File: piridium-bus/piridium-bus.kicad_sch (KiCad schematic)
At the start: 53 parts, among them J1 EPS, J2 MODEM UART, J3 ANT, J4 PAYLOAD, Q1 2N7002, Q2 DMP3015LSSQ, U1 LM1117-3.3, U2 TPS54394RSAR, U3 MAX6369, U4 74LS126, U5 DS3232M

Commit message: update routing
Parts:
- removed J4: PAYLOAD, Connector_Molex:Molex_Nano-Fit_105314-xx10_2x05_P2.50mm_Horizontal, symbol Connector_Generic:Conn_02x05_Top_Bottom
- added J4: PAYLOAD, Connector_PinHeader_2.54mm:PinHeader_2x05_P2.54mm_Vertical, symbol Connector_Generic:Conn_02x05_Odd_Even
- J1: footprint Connector_Molex:Molex_Nano-Fit_105313-xx04_1x04_P2.50mm_Horizontal -> Connector_PinHeader_2.54mm:PinHeader_1x04_P2.54mm_Horizontal
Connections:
- net +5V: no longer R9.1
- net +5VP: now also R9.1
- net GND: now also J4.10 (Pin_10), J4.9 (Pin_9); no longer A3.22 (RF_GND), J3.2 (Ext)
- net I2C_SCL: now also J4.2 (Pin_2)
- net I2C_SDA: now also J4.4 (Pin_4)
- net PAYLOAD_PWR: now also J4.1 (Pin_1)
- net SPI_CE0: now also J4.6 (Pin_6)
- net SPI_CE1: now also J4.8 (Pin_8)
- net SPI_MISO: now also J4.5 (Pin_5)
- net SPI_MOSI: now also J4.3 (Pin_3)
- net SPI_SCK: now also J4.7 (Pin_7)
- new net GNDS: A3.22 (RF_GND), J3.2 (Ext)
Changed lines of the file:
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@@
   (junction (at 248.92 55.88) (diameter 0) (color 0 0 0 0)
   )
-  (junction (at 236.22 133.35) (diameter 0) (color 0 0 0 0)
-  )
   (junction (at 20.32 114.3) (diameter 0) (color 0 0 0 0)
   )
@@
   (junction (at 50.8 50.8) (diameter 0) (color 0 0 0 0)
   )
-  (junction (at 236.22 125.73) (diameter 0) (color 0 0 0 0)
-  )
   (junction (at 179.07 77.47) (diameter 0) (color 0 0 0 0)
   )
@@
   )
   (junction (at 63.5 60.96) (diameter 0) (color 0 0 0 0)
+  )
+  (junction (at 246.38 128.27) (diameter 0) (color 0 0 0 0)
   )
   (junction (at 33.02 33.02) (diameter 0) (color 0 0 0 0)
@@
     (stroke (width 0) (type default) (color 0 0 0 0))
   )
-  (wire (pts (xy 246.38 128.27) (xy 246.38 133.35))
-    (stroke (width 0) (type default) (color 0 0 0 0))
-  )
   (polyline (pts (xy 231.14 83.82) (xy 231.14 45.72))
     (stroke (width 0) (type default) (color 0 0 0 0))
@@
     (stroke (width 0) (type default) (color 0 0 0 0))
   )
+  (wire (pts (xy 232.41 125.73) (xy 241.3 125.73))
+    (stroke (width 0) (type default) (color 0 0 0 0))
+  )
   (wire (pts (xy 45.72 133.35) (xy 49.53 133.35))
     (stroke (width 0) (type default) (color 0 0 0 0))
@@
     (stroke (width 0) (type default) (color 0 0 0 0))
   )
-  (wire (pts (xy 246.38 133.35) (xy 236.22 133.35))
-    (stroke (width 0) (type default) (color 0 0 0 0))
-  )
   (polyline (pts (xy 289.56 44.45) (xy 289.56 13.97))
     (stroke (width 0) (type default) (color 0 0 0 0))
@@
     (stroke (width 0) (type default) (color 0 0 0 0))
   )
-  (wire (pts (xy 232.41 125.73) (xy 236.22 125.73))
-    (stroke (width 0) (type default) (color 0 0 0 0))
-  )
   (wire (pts (xy 175.26 22.86) (xy 179.07 22.86))
     (stroke (width 0) (type default) (color 0 0 0 0))
@@
     (stroke (width 0) (type default) (color 0 0 0 0))
   )
-  (wire (pts (xy 236.22 133.35) (xy 236.22 125.73))
+  (wire (pts (xy 236.22 113.03) (xy 236.22 133.35))
     (stroke (width 0) (type default) (color 0 0 0 0))
   )
@@
     (stroke (width 0) (type default) (color 0 0 0 0))
   )
+  (wire (pts (xy 241.3 125.73) (xy 241.3 128.27))
+    (stroke (width 0) (type default) (color 0 0 0 0))
+  )
   (wire (pts (xy 240.03 99.06) (xy 242.57 99.06))
     (stroke (width 0) (type default) (color 0 0 0 0))
@@
     (stroke (width 0) (type default) (color 0 0 0 0))
   )
-  (wire (pts (xy 236.22 125.73) (xy 236.22 113.03))
-    (stroke (width 0) (type default) (color 0 0 0 0))
-  )
   (wire (pts (xy 179.07 69.85) (xy 179.07 77.47))
     (stroke (width 0) (type default) (color 0 0 0 0))
@@
   )
   (wire (pts (xy 99.06 57.15) (xy 114.3 57.15))
+    (stroke (width 0) (type default) (color 0 0 0 0))
+  )
+  (wire (pts (xy 241.3 128.27) (xy 246.38 128.27))
     (stroke (width 0) (type default) (color 0 0 0 0))
   )
@@
     (pin "1")
   )
+  (symbol (lib_id "power:GNDS") (at 246.38 128.27 0) (unit 1)
+    (in_bom yes) (on_board yes) (fields_autoplaced)
+    (property "Reference" "#PWR0101" (id 0) (at 246.38 134.62 0)
+      (effects (font (size 1.27 1.27)) hide)
+    )
+    (property "Value" "GNDS" (id 1) (at 246.38 133.35 0))
+    (property "Footprint" "" (id 2) (at 246.38 128.27 0)
+      (effects (font (size 1.27 1.27)) hide)
+    )
+    (property "Datasheet" "" (id 3) (at 246.38 128.27 0)
+      (effects (font (size 1.27 1.27)) hide)
+    )
+    (pin "1")
+  )
   (symbol (lib_id "power:GND") (at 25.4 99.06 0) (unit 1)
     (in_bom yes) (on_board yes)
@@
       (effects (font (size 1.27 1.27)) (justify left))
     )
-    (property "Footprint" "Connector_Molex:Molex_Nano-Fit_105313-xx04_1x04_P2.50mm_Horizontal" (id 2) (at 20.32 93.98 0)
+    (property "Footprint" "Connector_PinHeader_2.54mm:PinHeader_1x04_P2.54mm_Horizontal" (id 2) (at 20.32 93.98 0)
       (effects (font (size 1.27 1.27)) hide)
     )
@@
     (pin "2")
   )
+  (symbol (lib_id "power:+5VP") (at 233.68 91.44 0) (unit 1)
+    (in_bom yes) (on_board yes) (fields_autoplaced)
+    (property "Reference" "#PWR?" (id 0) (at 233.68 95.25 0)
+      (effects (font (size 1.27 1.27)) hide)
+    )
+    (property "Value" "+5VP" (id 1) (at 233.68 86.36 0))
+    (property "Footprint" "" (id 2) (at 233.68 91.44 0)
+      (effects (font (size 1.27 1.27)) hide)
+    )
+    (property "Datasheet" "" (id 3) (at 233.68 91.44 0)
+      (effects (font (size 1.27 1.27)) hide)
+    )
+    (pin "1")
+  )
   (symbol (lib_id "power:+5V") (at 114.3 69.85 90) (unit 1)
     (in_bom yes) (on_board yes) (fields_autoplaced)
@@
     )
     (pin "1")
-  )
-  (symbol (lib_id "Connector_Generic:Conn_02x05_Top_Bottom") (at 270.51 35.56 0) (unit 1)
-    (in_bom yes) (on_board yes) (fields_autoplaced)
-    (property "Reference" "J4" (id 0) (at 271.78 24.13 0))
-    (property "Value" "PAYLOAD" (id 1) (at 271.78 26.67 0))
-    (property "Footprint" "Connector_Molex:Molex_Nano-Fit_105314-xx10_2x05_P2.50mm_Horizontal" (id 2) (at 270.51 35.56 0)
-      (effects (font (size 1.27 1.27)) hide)
-    )
-    (property "Datasheet" "~" (id 3) (at 270.51 35.56 0)
-      (effects (font (size 1.27 1.27)) hide)
-    )
-    (pin "1")
-    (pin "10")
-    (pin "2")
-    (pin "3")
-    (pin "4")
-    (pin "5")
-    (pin "6")
-    (pin "7")
-    (pin "8")
-    (pin "9")
   )
   (symbol (lib_id "power:GND") (at 203.2 77.47 0) (unit 1)
@@
     (pin "2")
   )
+  (symbol (lib_id "Connector_Generic:Conn_02x05_Odd_Even") (at 270.51 35.56 0) (unit 1)
+    (in_bom yes) (on_board yes) (fields_autoplaced)
+    (property "Reference" "J4" (id 0) (at 271.78 24.13 0))
+    (property "Value" "PAYLOAD" (id 1) (at 271.78 26.67 0))
+    (property "Footprint" "Connector_PinHeader_2.54mm:PinHeader_2x05_P2.54mm_Vertical" (id 2) (at 270.51 35.56 0)
+      (effects (font (size 1.27 1.27)) hide)
+    )
+    (property "Datasheet" "~" (id 3) (at 270.51 35.56 0)
+      (effects (font (size 1.27 1.27)) hide)
+    )
+    (pin "1")
+    (pin "10")
+    (pin "2")
+    (pin "3")
+    (pin "4")
+    (pin "5")
+    (pin "6")
+    (pin "7")
+    (pin "8")
+    (pin "9")
+  )
   (symbol (lib_id "Device:R") (at 234.95 21.59 0) (mirror y) (unit 1)
     (in_bom yes) (on_board yes)
@@
     (pin "1")
   )
-  (symbol (lib_id "power:+5V") (at 233.68 91.44 0) (unit 1)
-    (in_bom yes) (on_board yes) (fields_autoplaced)
-    (property "Reference" "#PWR028" (id 0) (at 233.68 95.25 0)
-      (effects (font (size 1.27 1.27)) hide)
-    )
-    (property "Value" "+5V" (id 1) (at 233.68 86.36 0))
-    (property "Footprint" "" (id 2) (at 233.68 91.44 0)
-      (effects (font (size 1.27 1.27)) hide)
-    )
-    (property "Datasheet" "" (id 3) (at 233.68 91.44 0)
-      (effects (font (size 1.27 1.27)) hide)
-    )
-    (pin "1")
-  )
   (symbol (lib_id "power:GND") (at 236.22 133.35 0) (unit 1)
     (in_bom yes) (on_board yes) (fields_autoplaced)
@@
       (reference "#PWR027") (unit 1) (value "GND") (footprint "")
     )
-    (path "/fb473a15-78ef-46d6-8141-4de438a4d939"
-      (reference "#PWR028") (unit 1) (value "+5V") (footprint "")
-    )
     (path "/2957e5e6-b93f-4726-81ca-ef39d24a291b"
       (reference "#PWR029") (unit 1) (value "GND") (footprint "")
@@
       (reference "#PWR036") (unit 1) (value "GND") (footprint "")
     )
+    (path "/2408a518-0026-450c-95ff-4703dcc60255"
+      (reference "#PWR0101") (unit 1) (value "GNDS") (footprint "")
+    )
+    (path "/733fde0d-fd57-4432-87d0-a513bd1e831a"
+      (reference "#PWR?") (unit 1) (value "+5VP") (footprint "")
+    )
     (path "/dee1721c-7498-4aa5-ba4d-8809f87db910"
       (reference "A1") (unit 1) (value "Raspberry_Pi_Zero") (footprint "piridium-bus:Raspberry Pi Zero")
@@
     )
     (path "/321ea199-1ef7-40a0-ade9-c079749b846a"
-      (reference "J1") (unit 1) (value "EPS") (footprint "Connector_Molex:Molex_Nano-Fit_105313-xx04_1x04_P2.50mm_Horizontal")
+      (reference "J1") (unit 1) (value "EPS") (footprint "Connector_PinHeader_2.54mm:PinHeader_1x04_P2.54mm_Horizontal")
     )
     (path "/8c75ddb9-a755-44c9-bc38-54adf2375e84"
@@
       (reference "J3") (unit 1) (value "ANT") (footprint "Connector_Coaxial:SMA_Amphenol_901-144_Vertical")
     )
-    (path "/c327fdf2-43a7-41a6-a455-95be41197291"
-      (reference "J4") (unit 1) (value "PAYLOAD") (footprint "Connector_Molex:Molex_Nano-Fit_105314-xx10_2x05_P2.50mm_Horizontal")
+    (path "/e777e5ce-0d5c-4bac-a8bd-4486133c1e81"
+      (reference "J4") (unit 1) (value "PAYLOAD") (footprint "Connector_PinHeader_2.54mm:PinHeader_2x05_P2.54mm_Vertical")
     )
     (path "/f194e39b-0e91-4755-8253-375d1bf0a961"

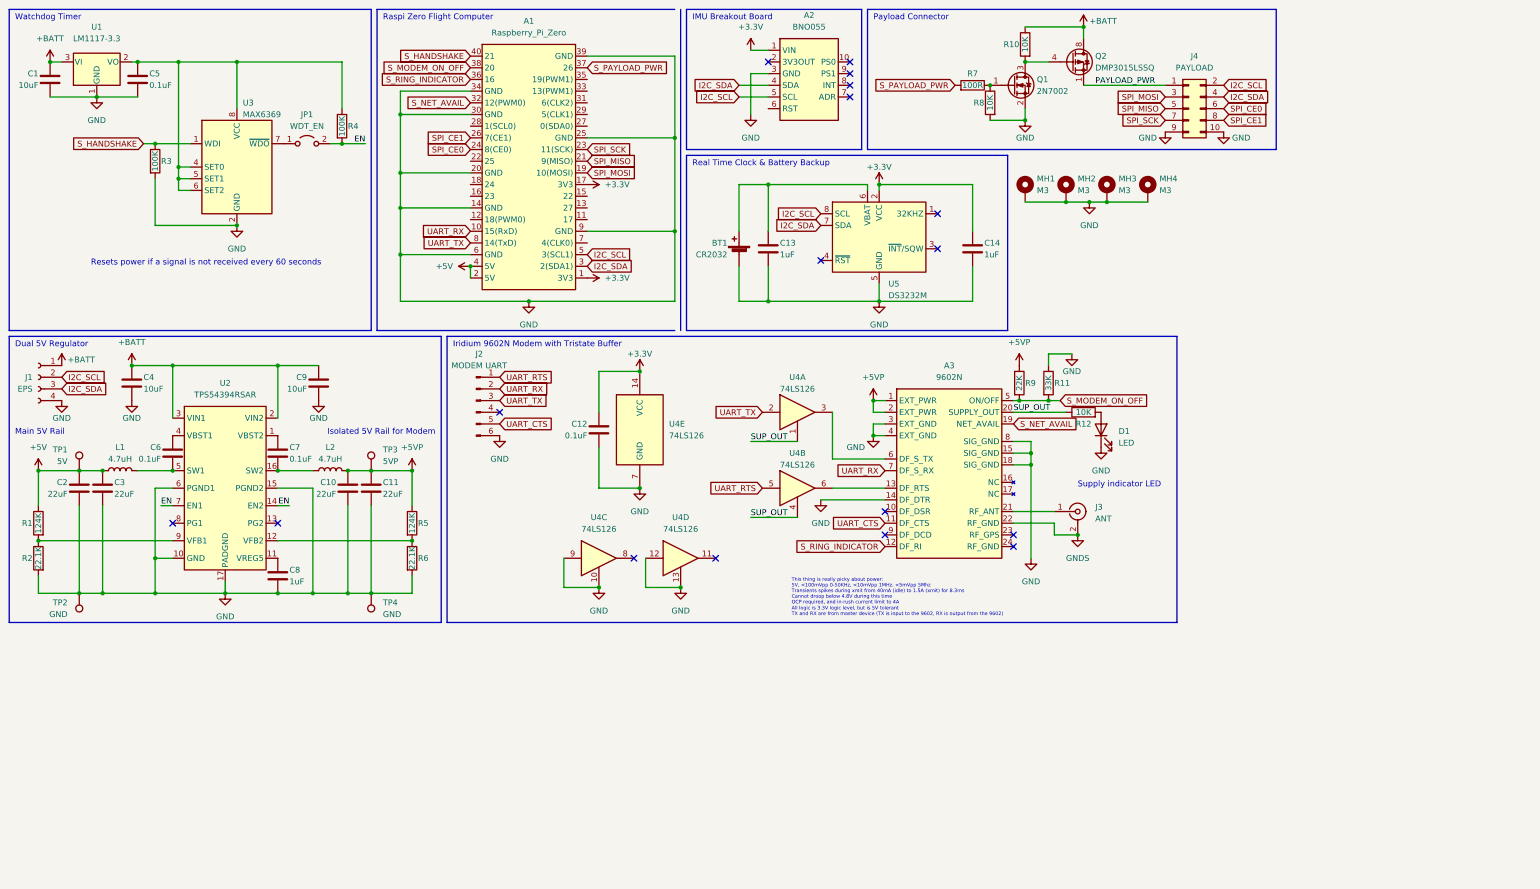
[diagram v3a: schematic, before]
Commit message: add inhibits, telemetry, and solar to bus
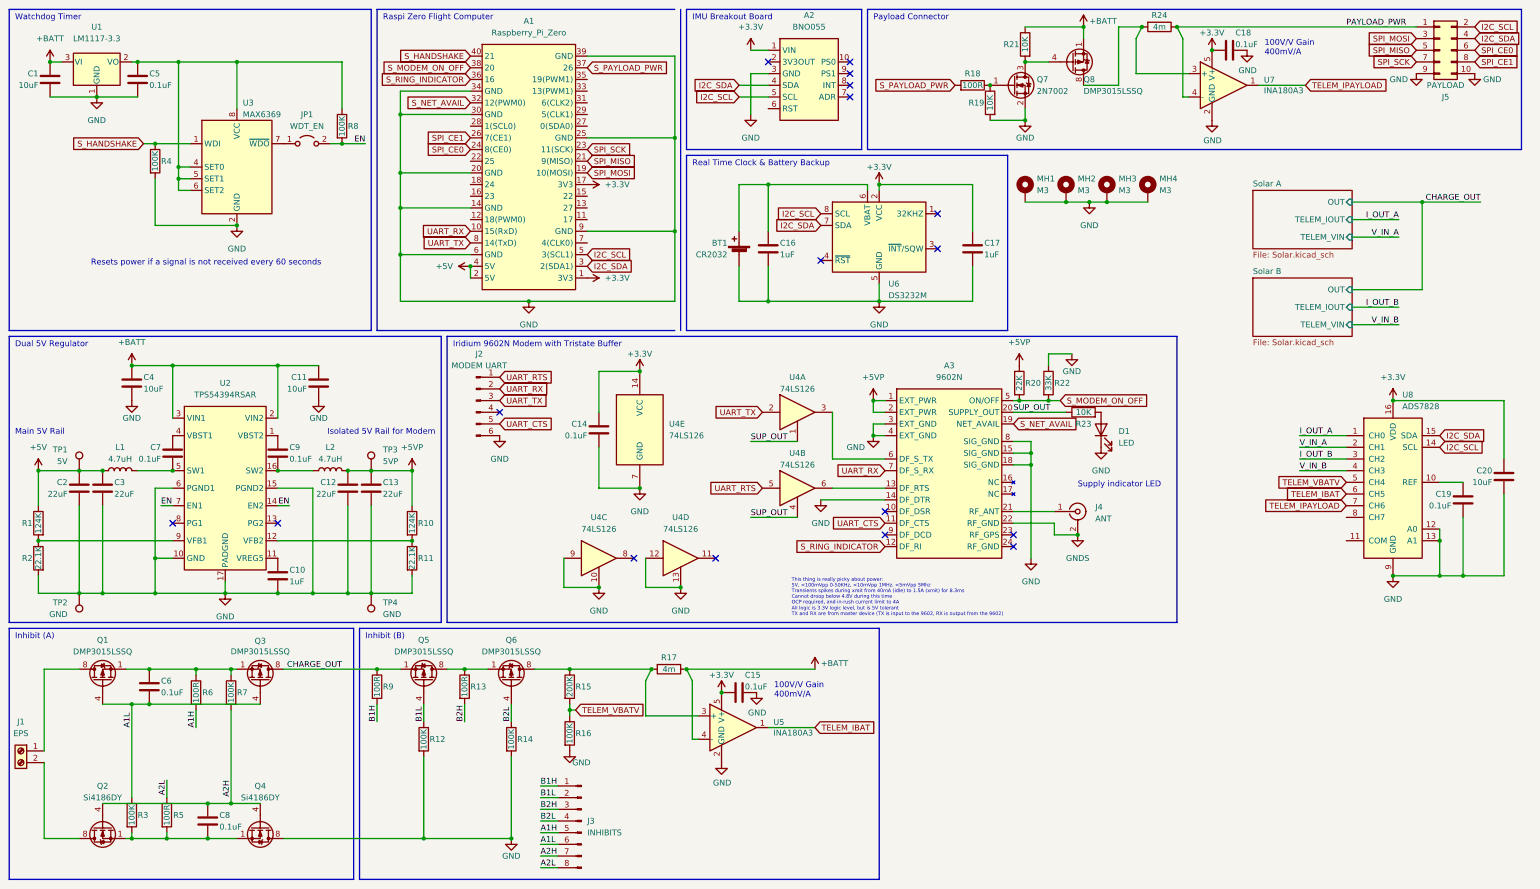
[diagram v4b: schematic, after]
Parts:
- removed J1: EPS, Connector_PinHeader_2.54mm:PinHeader_1x04_P2.54mm_Horizontal, symbol Connector:Conn_01x04_Female
- added C15, C18, C19, C6, C8: 0.1uF, Capacitor_SMD:C_0805_2012Metric, symbol Device:C
- added C20: 10uF, Capacitor_SMD:C_0805_2012Metric, symbol Device:C
- added J1: EPS, TerminalBlock_Phoenix:TerminalBlock_Phoenix_PT-1,5-2-3.5-H_1x02_P3.50mm_Horizontal, symbol Connector:Screw_Terminal_01x02
- added J3: INHIBITS, Connector_PinHeader_2.54mm:PinHeader_1x08_P2.54mm_Horizontal, symbol Connector:Conn_01x08_Male
- added Q1, Q3, Q5, Q6: DMP3015LSSQ, Package_SO:SOIC-8_3.9x4.9mm_P1.27mm, symbol Transistor_FET:IRF7404
- added Q2, Q4: Si4186DY, Package_SO:SOIC-8_3.9x4.9mm_P1.27mm, symbol Transistor_FET:Si4162DY
- added R12, R14, R16, R3, R7: 100K, Resistor_SMD:R_0805_2012Metric, symbol Device:R
- added R13, R5, R6, R9: 100R, Resistor_SMD:R_0805_2012Metric, symbol Device:R
- added R15: 200K, Resistor_SMD:R_0805_2012Metric, symbol Device:R
- added R17, R24: 4m, Resistor_SMD:R_1206_3216Metric, symbol Device:R
- added U5, U7: INA180A3, Package_TO_SOT_SMD:SOT-23-5, symbol Amplifier_Current:INA138
- added U8: ADS7828, Package_SO:TSSOP-16_4.4x5mm_P0.65mm, symbol Analog_ADC:ADS7828
- J5: renamed from J4; footprint Connector_PinHeader_2.54mm:PinHeader_2x05_P2.54mm_Vertical -> Connector_IDC:IDC-Header_2x05_P2.54mm_Vertical
- renumbered C8 to C10, C9 to C11, C10 to C12, C11 to C13, C12 to C14, C13 to C16, C14 to C17, C6 to C7, C7 to C9, J3 to J4, Q1 to Q7, Q2 to Q8, R5 to R10, R6 to R11, R7 to R18, R8 to R19, R9 to R20, R10 to R21, R11 to R22, R12 to R23, R3 to R4, R4 to R8, U5 to U6
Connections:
- net +3.3V: now also C15.1, C18.1, C20.1, U5.5 (V+), U7.5 (V+), U8.16 (VDD)
- net +BATT: now also Q8.1 (S), Q8.2 (S), Q8.3 (S), R17.1, U5.4 (-); no longer Q8.5 (D), Q8.6 (D), Q8.7 (D), Q8.8 (D)
- net GND: now also C15.2, C18.2, C19.2, C20.2, Q4.5 (D), Q4.6 (D), Q4.7 (D), Q4.8 (D), R12.2, R14.2, R16.2, U5.2 (GND), U7.2 (GND), U8.12 (A0), U8.13 (A1), U8.9 (GND)
- net I2C_SCL: now also U8.14 (SCL)
- net I2C_SDA: now also U8.15 (SDA)
- net PAYLOAD_PWR: now also R24.1, U7.4 (-); no longer Q8.1 (S), Q8.2 (S), Q8.3 (S)
- new net: C19.1, U8.10 (REF)
- new net: Q6.5 (D), Q6.6 (D), Q6.7 (D), Q6.8 (D), R15.1, R17.2, U5.3 (+)
- new net: C8.2, Q2.1 (S), Q2.2 (S), Q2.3 (S), Q4.1 (S), Q4.2 (S), Q4.3 (S), R3.2, R5.2
- new net: J1.2 (Pin_2), Q2.5 (D), Q2.6 (D), Q2.7 (D), Q2.8 (D)
- new net: C6.1, Q1.1 (S), Q1.2 (S), Q1.3 (S), Q3.1 (S), Q3.2 (S), Q3.3 (S), R6.1, R7.1
- new net: J1.1 (Pin_1), Q1.5 (D), Q1.6 (D), Q1.7 (D), Q1.8 (D)
- new net: Q5.5 (D), Q5.6 (D), Q5.7 (D), Q5.8 (D), Q6.1 (S), Q6.2 (S), Q6.3 (S), R13.1
- new net: Q8.5 (D), Q8.6 (D), Q8.7 (D), Q8.8 (D), R24.2, U7.3 (+)
- new net A1H: J3.5 (Pin_5), R6.2
- new net A1L: C6.2, J3.6 (Pin_6), Q1.4 (G), Q3.4 (G), R3.1
- new net A2H: C8.1, J3.7 (Pin_7), Q2.4 (G), Q4.4 (G), R7.2
- new net A2L: J3.8 (Pin_8), R5.1
- new net B1H: J3.1 (Pin_1), R9.2
- new net B1L: J3.2 (Pin_2), Q5.4 (G), R12.1
- new net B2H: J3.3 (Pin_3), R13.2
- new net B2L: J3.4 (Pin_4), Q6.4 (G), R14.1
- new net CHARGE_OUT: Q3.5 (D), Q3.6 (D), Q3.7 (D), Q3.8 (D), Q5.1 (S), Q5.2 (S), Q5.3 (S), R9.1
- new net I_OUT_A: U8.1 (CH0)
- new net I_OUT_B: U8.3 (CH2)
- new net TELEM_IBAT: U5.1, U8.6 (CH5)
- new net TELEM_IPAYLOAD: U7.1, U8.7 (CH6)
- new net TELEM_VBATV: R15.2, R16.1, U8.5 (CH4)
- new net V_IN_A: U8.2 (CH1)
- new net V_IN_B: U8.4 (CH3)
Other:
- added sheet Solar A (Solar.kicad_sch)
- added sheet Solar B (Solar.kicad_sch)
- note added: "100V/V Gain 400mV/A"
- note added: "Inhibit (A)"
- note added: "Inhibit (B)"
- moved on the sheet: J5

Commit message: fix bus board messup, remove redundant components from eps
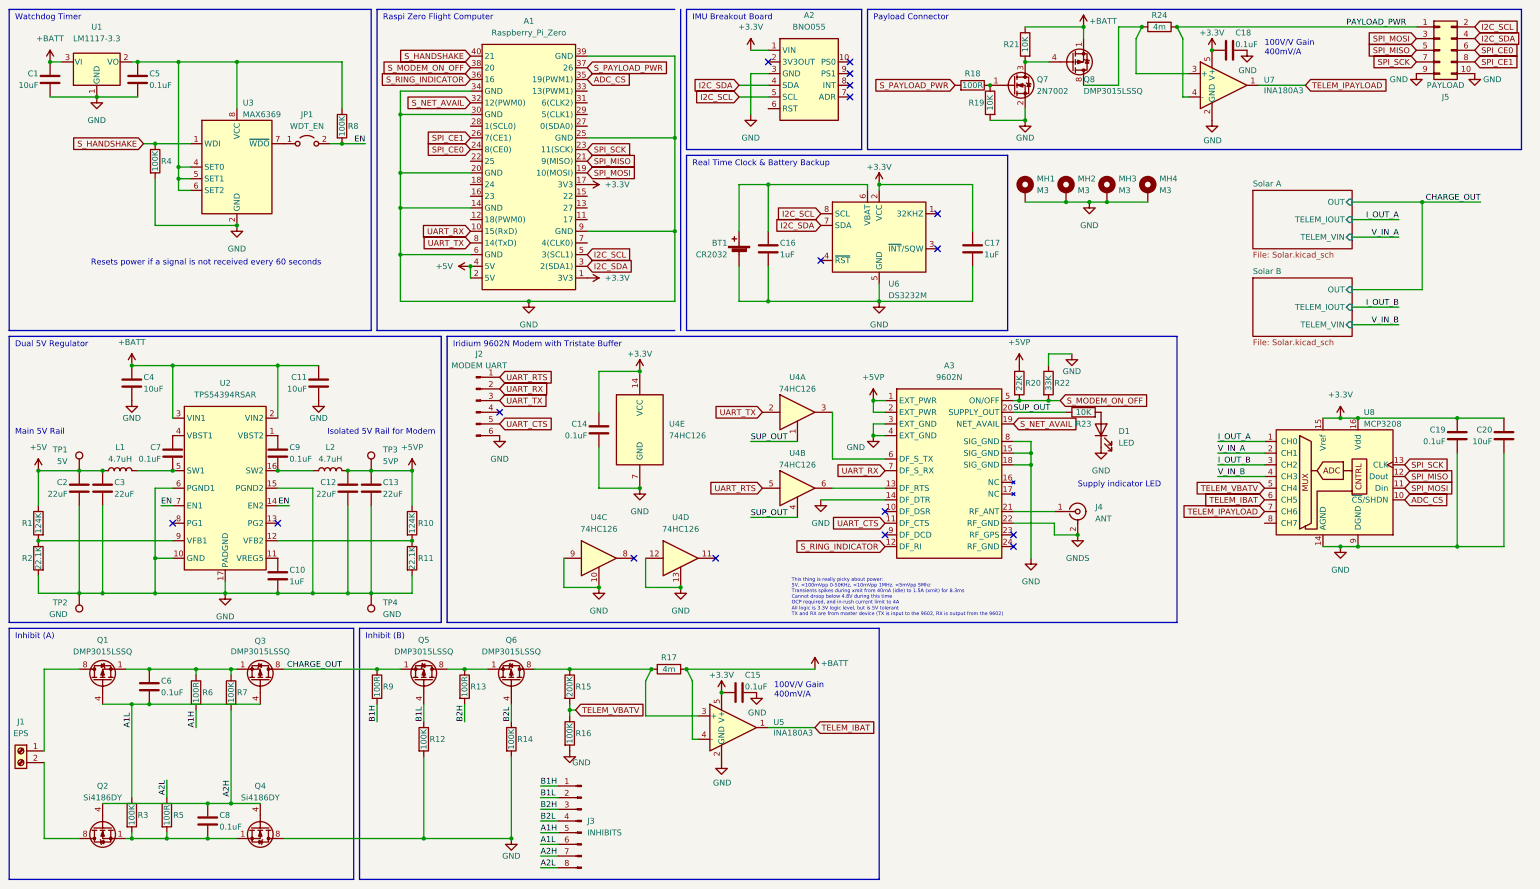
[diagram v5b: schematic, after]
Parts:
- removed U8: ADS7828, Package_SO:TSSOP-16_4.4x5mm_P0.65mm, symbol Analog_ADC:ADS7828
- added U8: MCP3208, symbol Analog_ADC:MCP3208
- U4: value 74LS126 -> 74HC126
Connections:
- net +3.3V: now also C19.1, U8.15 (Vref), U8.16 (Vdd)
- net GND: now also U8.14 (AGND), U8.9 (DGND)
- net I_OUT_A: now also U8.1 (CH0)
- net I_OUT_B: now also U8.3 (CH2)
- net SPI_MISO: now also U8.12 (Dout)
- net SPI_MOSI: now also U8.11 (Din)
- net SPI_SCK: now also U8.13 (CLK)
- net TELEM_IBAT: now also U8.6 (CH5)
- net TELEM_IPAYLOAD: now also U8.7 (CH6)
- net TELEM_VBATV: now also U8.5 (CH4)
- net V_IN_A: now also U8.2 (CH1)
- net V_IN_B: now also U8.4 (CH3)
- net ADC_CS: now reaches A1.35 (19(PWM1))
- net ADC_CS: now also U8.10 (~{CS}/SHDN)
